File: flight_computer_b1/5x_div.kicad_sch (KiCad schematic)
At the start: 2 parts

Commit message: flight computer: added pyro circuit and digikey part numbers
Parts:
- R42: DIGIKEY PART N (none) -> YAG1237CT-ND
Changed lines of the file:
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@@
+			)
+		)
+		(property "DIGIKEY PART N" "YAG1237CT-ND"
+			(at 138.43 88.9 0)
+			(effects
+				(font
+					(size 1.27 1.27)
+				)
+				(hide yes)
 			)
 		)
@@
 			(at 138.43 76.2 0)
 			(effects
+				(font
+					(size 1.27 1.27)
+				)
+				(hide yes)
+			)
+		)
+		(property "DIGIKEY PART N" ""
+			(at 138.43 76.2 0)
+			(effects

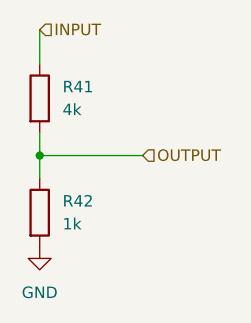
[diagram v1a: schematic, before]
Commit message: flight computer: new ideal diode, small schematic changes
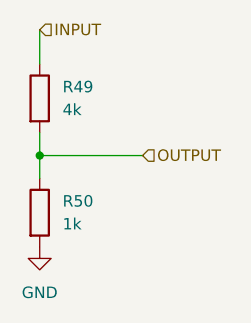
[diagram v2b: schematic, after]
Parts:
- renumbered R41 to R49, R42 to R50
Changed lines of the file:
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@@
 		(dnp no)
 		(fields_autoplaced yes)
-		(property "Reference" "R42"
+		(property "Reference" "R50"
 			(at 140.97 87.6299 0)
 			(effects
@@
 		(instances
 			(project "flight_computer"
-				(path "/b71a7b79-cdb5-4e38-a72c-0daaa3474f05/029c0f5b-a791-4164-8d50-d62e9084bdcb"
-					(reference "R46")
-					(unit 1)
-				)
-				(path "/b71a7b79-cdb5-4e38-a72c-0daaa3474f05/620cf1fc-ff4d-47fa-ab04-d5fa47e47558"
-					(reference "R42")
-					(unit 1)
-				)
 				(path "/b71a7b79-cdb5-4e38-a72c-0daaa3474f05/928b9f1b-24ea-477b-818e-bdb9528e433c"
 					(reference "R50")
-					(unit 1)
-				)
-				(path "/b71a7b79-cdb5-4e38-a72c-0daaa3474f05/de2783c8-9f85-4a38-b63f-fdf618754a5a"
-					(reference "R44")
-					(unit 1)
-				)
-				(path "/b71a7b79-cdb5-4e38-a72c-0daaa3474f05/ef83cc16-0363-45ff-9c72-b8e322ba88b6"
-					(reference "R48")
 					(unit 1)
 				)
@@
 		(dnp no)
 		(fields_autoplaced yes)
-		(property "Reference" "#PWR058"
+		(property "Reference" "#PWR062"
 			(at 138.43 99.06 0)
 			(effects
@@
 		(instances
 			(project "flight_computer"
-				(path "/b71a7b79-cdb5-4e38-a72c-0daaa3474f05/029c0f5b-a791-4164-8d50-d62e9084bdcb"
-					(reference "#PWR060")
-					(unit 1)
-				)
-				(path "/b71a7b79-cdb5-4e38-a72c-0daaa3474f05/620cf1fc-ff4d-47fa-ab04-d5fa47e47558"
-					(reference "#PWR058")
-					(unit 1)
-				)
 				(path "/b71a7b79-cdb5-4e38-a72c-0daaa3474f05/928b9f1b-24ea-477b-818e-bdb9528e433c"
 					(reference "#PWR062")
-					(unit 1)
-				)
-				(path "/b71a7b79-cdb5-4e38-a72c-0daaa3474f05/de2783c8-9f85-4a38-b63f-fdf618754a5a"
-					(reference "#PWR059")
-					(unit 1)
-				)
-				(path "/b71a7b79-cdb5-4e38-a72c-0daaa3474f05/ef83cc16-0363-45ff-9c72-b8e322ba88b6"
-					(reference "#PWR061")
 					(unit 1)
 				)
@@
 		(dnp no)
 		(fields_autoplaced yes)
-		(property "Reference" "R41"
+		(property "Reference" "R49"
 			(at 140.97 74.9299 0)
 			(effects
@@
 		(instances
 			(project "flight_computer"
-				(path "/b71a7b79-cdb5-4e38-a72c-0daaa3474f05/029c0f5b-a791-4164-8d50-d62e9084bdcb"
-					(reference "R45")
-					(unit 1)
-				)
-				(path "/b71a7b79-cdb5-4e38-a72c-0daaa3474f05/620cf1fc-ff4d-47fa-ab04-d5fa47e47558"
-					(reference "R41")
-					(unit 1)
-				)
 				(path "/b71a7b79-cdb5-4e38-a72c-0daaa3474f05/928b9f1b-24ea-477b-818e-bdb9528e433c"
 					(reference "R49")
 					(unit 1)
 				)
-				(path "/b71a7b79-cdb5-4e38-a72c-0daaa3474f05/de2783c8-9f85-4a38-b63f-fdf618754a5a"
-					(reference "R43")
-					(unit 1)
-				)
-				(path "/b71a7b79-cdb5-4e38-a72c-0daaa3474f05/ef83cc16-0363-45ff-9c72-b8e322ba88b6"
-					(reference "R47")
-					(unit 1)
-				)
